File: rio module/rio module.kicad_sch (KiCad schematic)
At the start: 11 parts, among them J1 MTJ-88ARX1-FSM-LG, J2 MTJ-88ARX1-FSM-LG, J3 Conn_01x02_Pin, J4 Conn_01x02_Pin, J5 Conn_01x02_Pin, J6 Conn_01x02_Pin, J7 Conn_01x02_Pin, SW1 SW_DPST

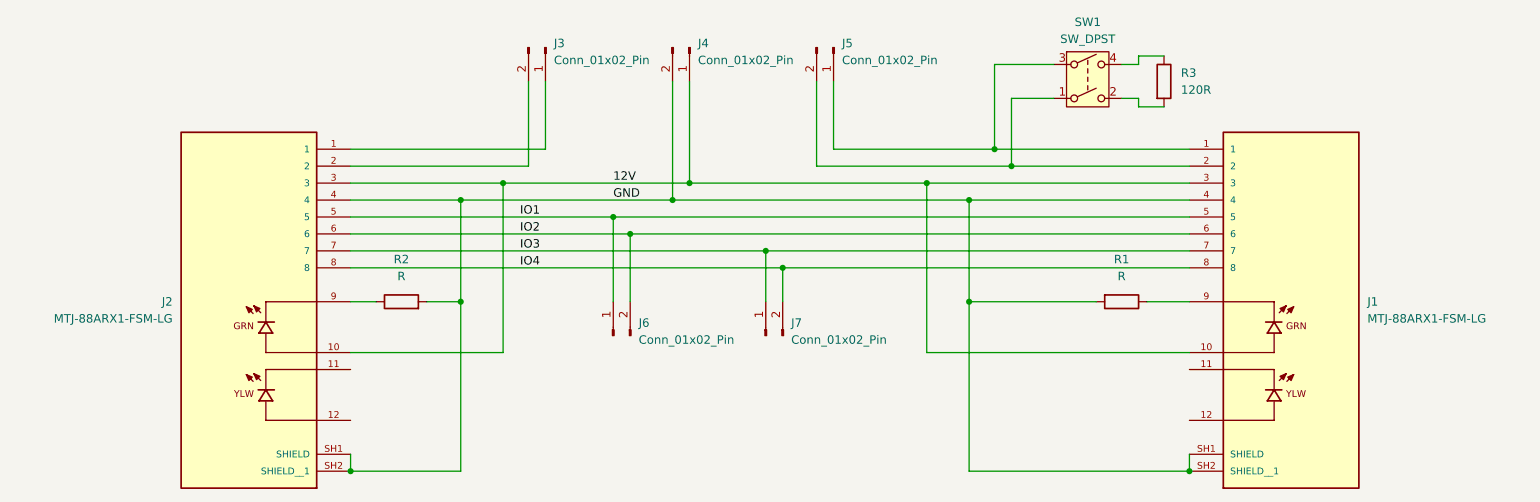
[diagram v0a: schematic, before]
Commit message: removed mxp crossover, moved to hardwired DIO, switching from DIO WAGOs to Molex SL
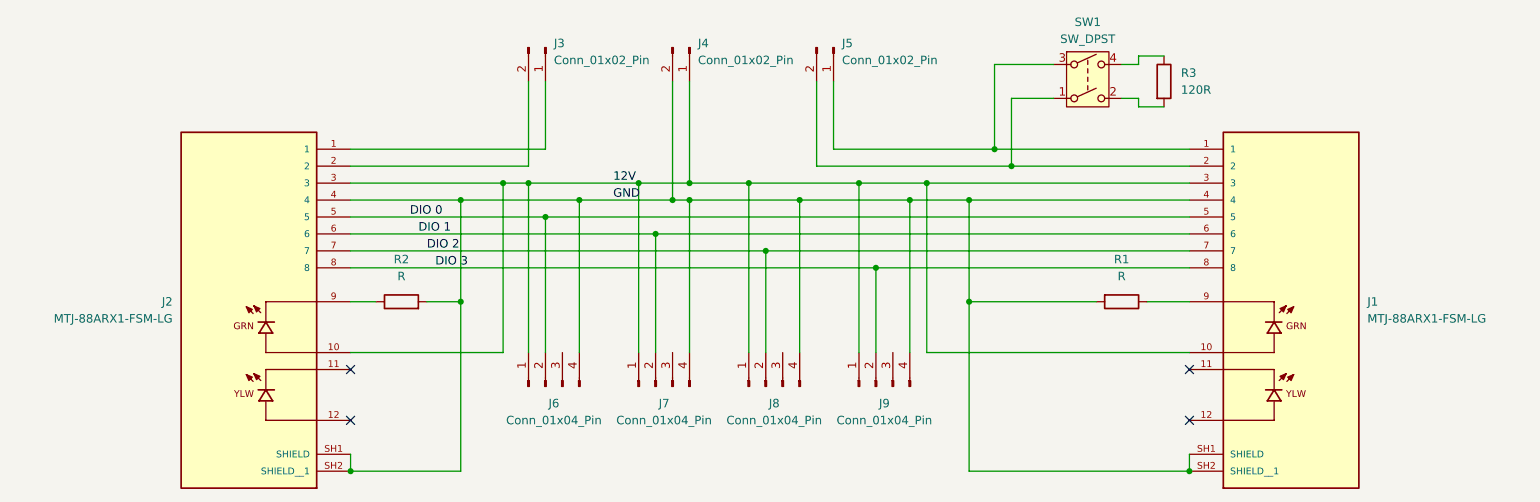
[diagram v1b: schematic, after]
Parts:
- removed J6, J7: Conn_01x02_Pin, custom:TerminalBlock_WAGO_2601-1102_1x02_P3.50mm_Horizontal w-model, symbol Connector:Conn_01x02_Pin
- added J6, J7, J8, J9: Conn_01x04_Pin, custom:Molex_SL_171971-0004_1x04_P2.54mm_Vertical, symbol Connector:Conn_01x04_Pin
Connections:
- net 12V: now also J6.1 (Pin_1), J7.1 (Pin_1), J8.1 (Pin_1), J9.1 (Pin_1)
- net GND: now also J6.4 (Pin_4), J7.4 (Pin_4), J8.4 (Pin_4), J9.4 (Pin_4)
- net IO1 renamed DIO 0
- net DIO 0: now also J6.2 (Pin_2)
- net IO2 renamed DIO 1
- net DIO 1: now also J7.2 (Pin_2)
- net IO3 renamed DIO 2
- net DIO 2: now also J8.2 (Pin_2)
- net IO4 renamed DIO 3
- net DIO 3: now also J9.2 (Pin_2)
- no-connect marks 0 -> 4
